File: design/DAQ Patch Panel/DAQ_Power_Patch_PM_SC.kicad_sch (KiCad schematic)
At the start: 8 parts, among them J1 Sensor 1 Terminal, J2 GND, J4 Voltage Input Terminal, J5 Sensor 1 Output, SW1 SW_SP3T, SW2 SW_SPDT_MSM

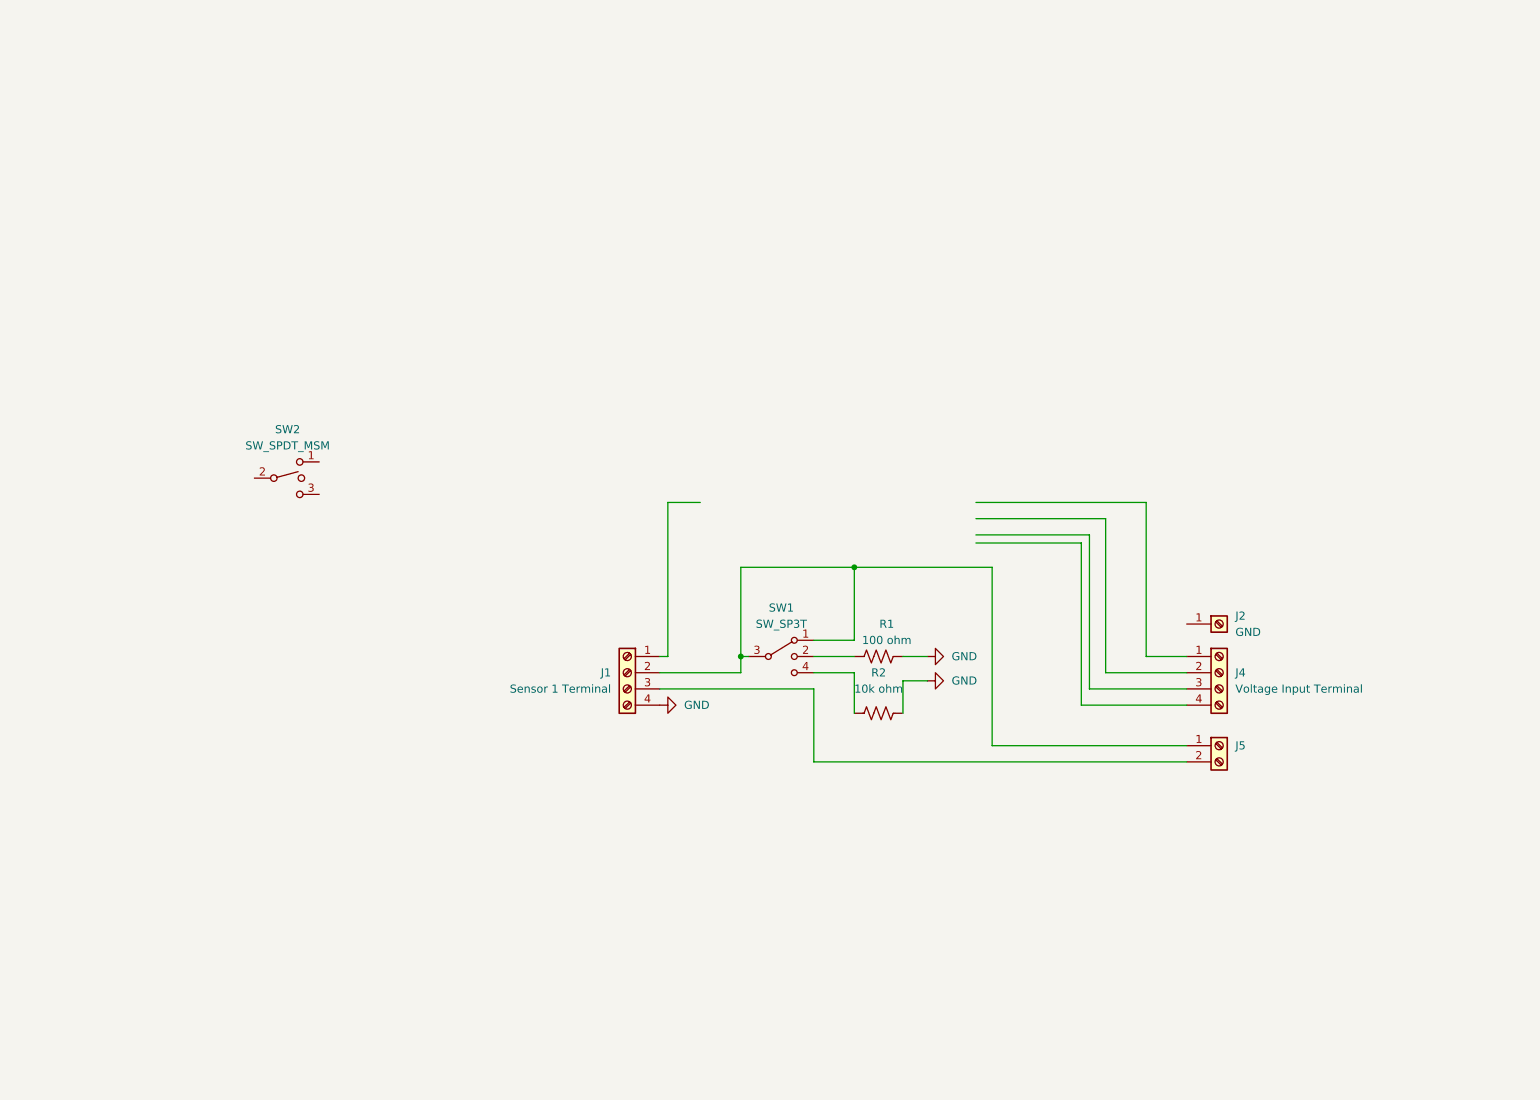
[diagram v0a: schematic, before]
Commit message: Changes to delete switches and duplicate board setup
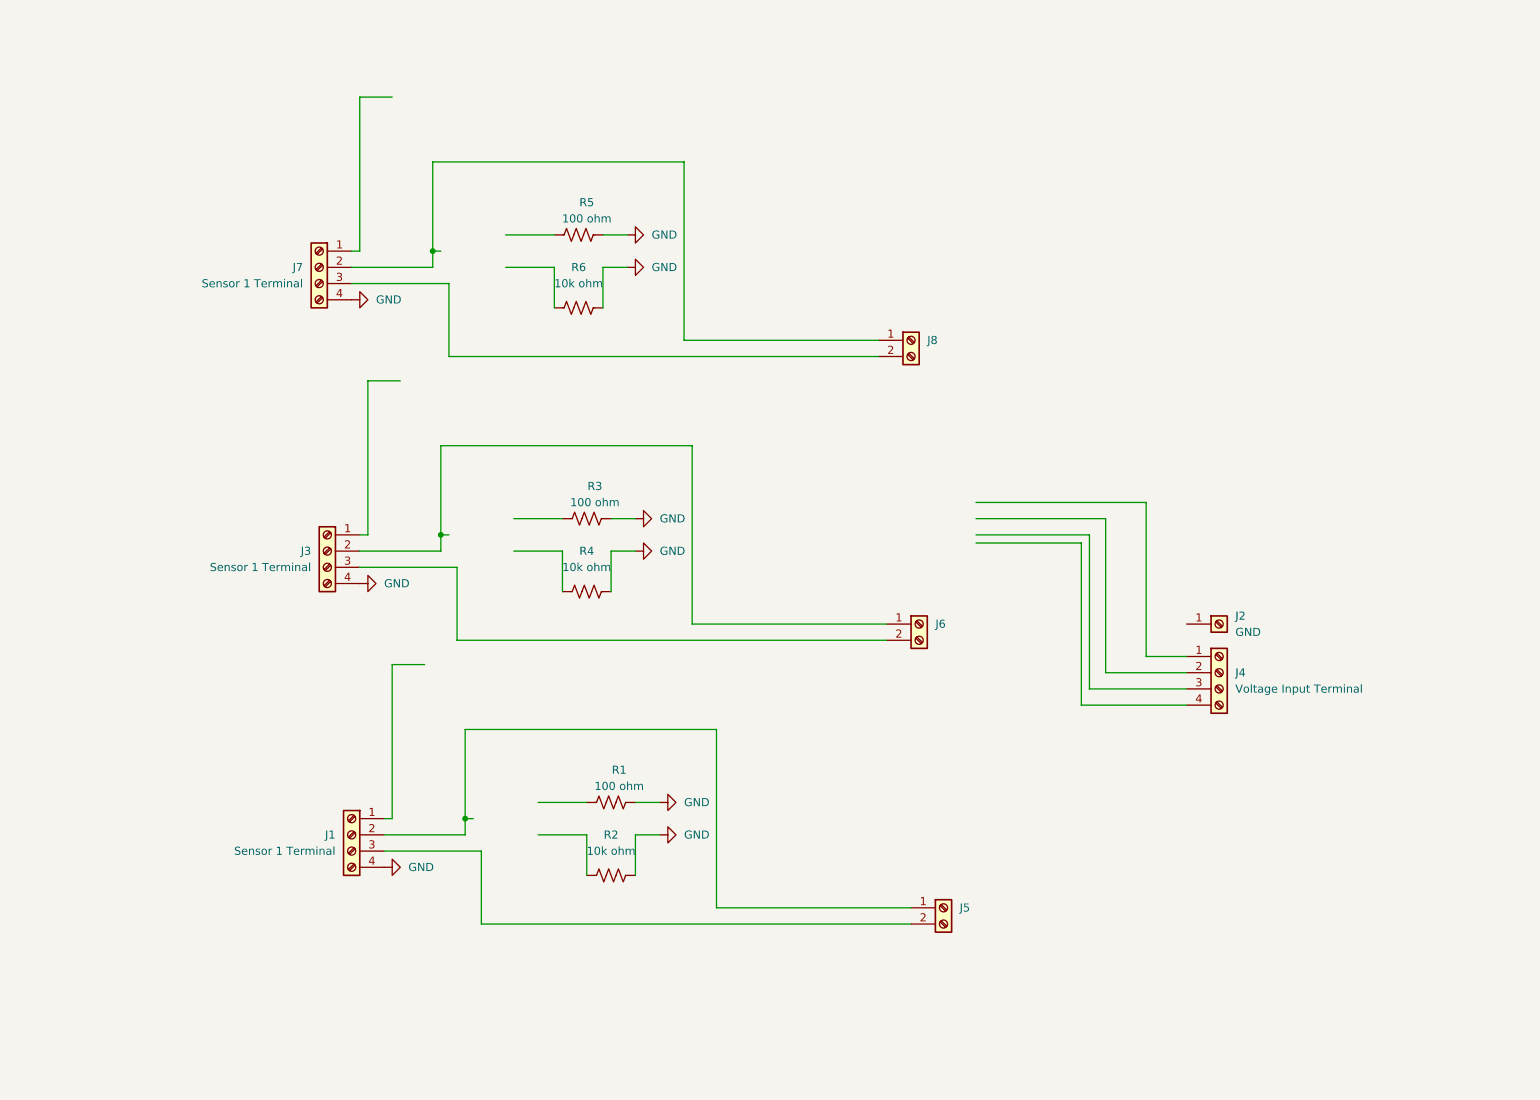
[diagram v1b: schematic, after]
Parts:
- removed SW1: SW_SP3T, symbol Switch:SW_SP3T
- removed SW2: SW_SPDT_MSM, symbol Switch:SW_SPDT_MSM
- added J3, J7: Sensor 1 Terminal, symbol Connector:Screw_Terminal_01x04
- added J6, J8: Sensor 1 Output, symbol Connector:Screw_Terminal_01x02
- added R3, R5: 100 ohm, symbol Device:R_US
- added R4, R6: 10k ohm, symbol Device:R_US
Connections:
- net GND: now also J3.4 (Pin_4), J7.4 (Pin_4), R3.2, R4.2, R5.2, R6.2
- new net: J3.2 (Pin_2), J6.1 (Pin_1)
- new net: J3.3 (Pin_3), J6.2 (Pin_2)
- new net: J7.2 (Pin_2), J8.1 (Pin_1)
- new net: J7.3 (Pin_3), J8.2 (Pin_2)
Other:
- moved on the sheet: J1, J5, R1, R2

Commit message: Added Jumpers
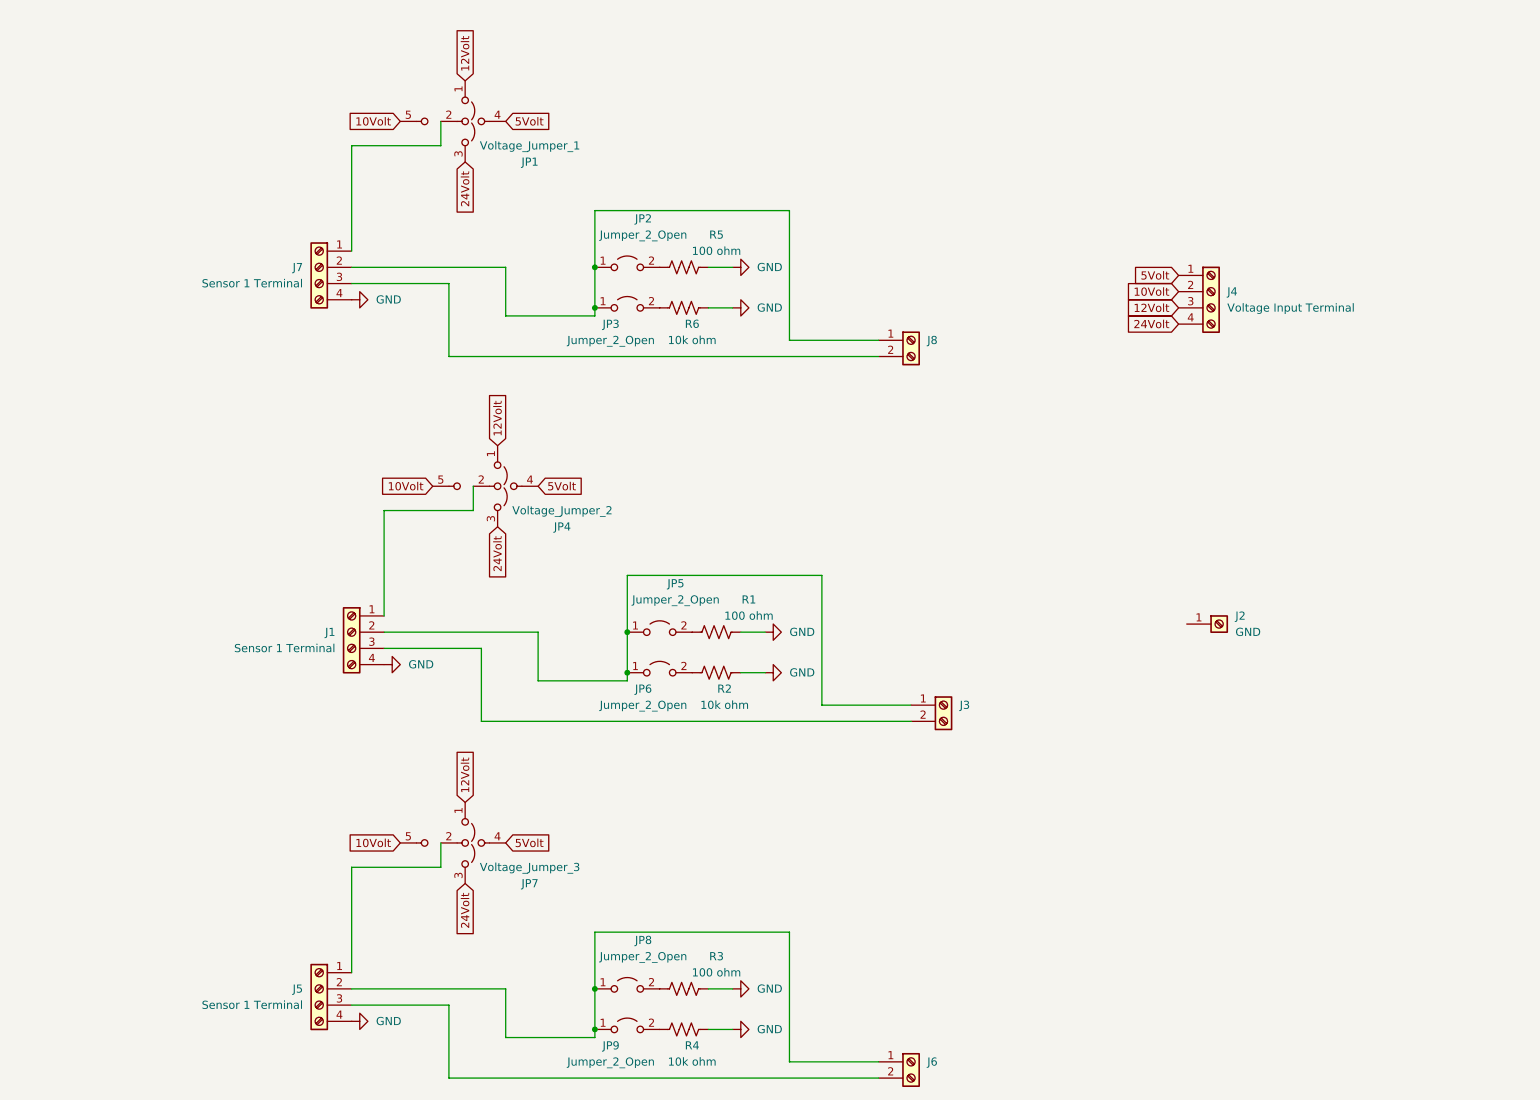
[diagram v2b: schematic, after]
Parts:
- removed J3: Sensor 1 Terminal, symbol Connector:Screw_Terminal_01x04
- removed J5: Sensor 1 Output, symbol Connector:Screw_Terminal_01x02
- added J3: Sensor 1 Output, symbol Connector:Screw_Terminal_01x02
- added J5: Sensor 1 Terminal, symbol Connector:Screw_Terminal_01x04
- added JP1: Voltage_Jumper_1, symbol Jumper:Jumper_3_Open
- added JP2, JP3, JP5, JP6, JP8, JP9: Jumper_2_Open, symbol Jumper:Jumper_2_Open
- added JP4: Voltage_Jumper_2, symbol Jumper:Jumper_3_Open
- added JP7: Voltage_Jumper_3, symbol Jumper:Jumper_3_Open
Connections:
- net GND: now also J5.4 (Pin_4)
- net 5Volt: now reaches J4.1 (Pin_1)
- net 5Volt: now also JP1.4 (C), JP4.4 (C), JP7.4 (C)
- net 10Volt: now reaches J4.2 (Pin_2)
- net 10Volt: now also JP1.5 (C), JP4.5 (C), JP7.5 (C)
- net 12Volt: now reaches J4.3 (Pin_3)
- net 12Volt: now also JP1.1 (A), JP4.1 (A), JP7.1 (A)
- net 24Volt: now reaches J4.4 (Pin_4)
- net 24Volt: now also JP1.3 (B), JP4.3 (B), JP7.3 (B)
- net at J1.2 (Pin_2): now also J3.1 (Pin_1), JP5.1 (A), JP6.1 (A)
- net at J1.3 (Pin_3): now also J3.2 (Pin_2)
- net at R2.1: now also JP6.2 (B)
- net at J6.1 (Pin_1): now also J5.2 (Pin_2), JP8.1 (A), JP9.1 (A)
- net at J6.2 (Pin_2): now also J5.3 (Pin_3)
- net at J1.1 (Pin_1): now also JP4.2 (C)
- net at J7.2 (Pin_2), J8.1 (Pin_1): now also JP2.1 (A), JP3.1 (A)
- net at R1.1: now also JP5.2 (B)
- net at R3.1: now also JP8.2 (B)
- net at R4.1: now also JP9.2 (B)
- net at R5.1: now also JP2.2 (B)
- net at R6.1: now also JP3.2 (B)
- net at J7.1 (Pin_1): now also JP1.2 (C)
- new net: J5.1 (Pin_1), JP7.2 (C)
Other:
- moved on the sheet: J4, R5, R6

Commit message: Connection for 2 thermistors or 4-20 amp sensors
Added option for 4th connector to also be power port and doubled resistors to allow for two thermistors or 4-20 amp sensors
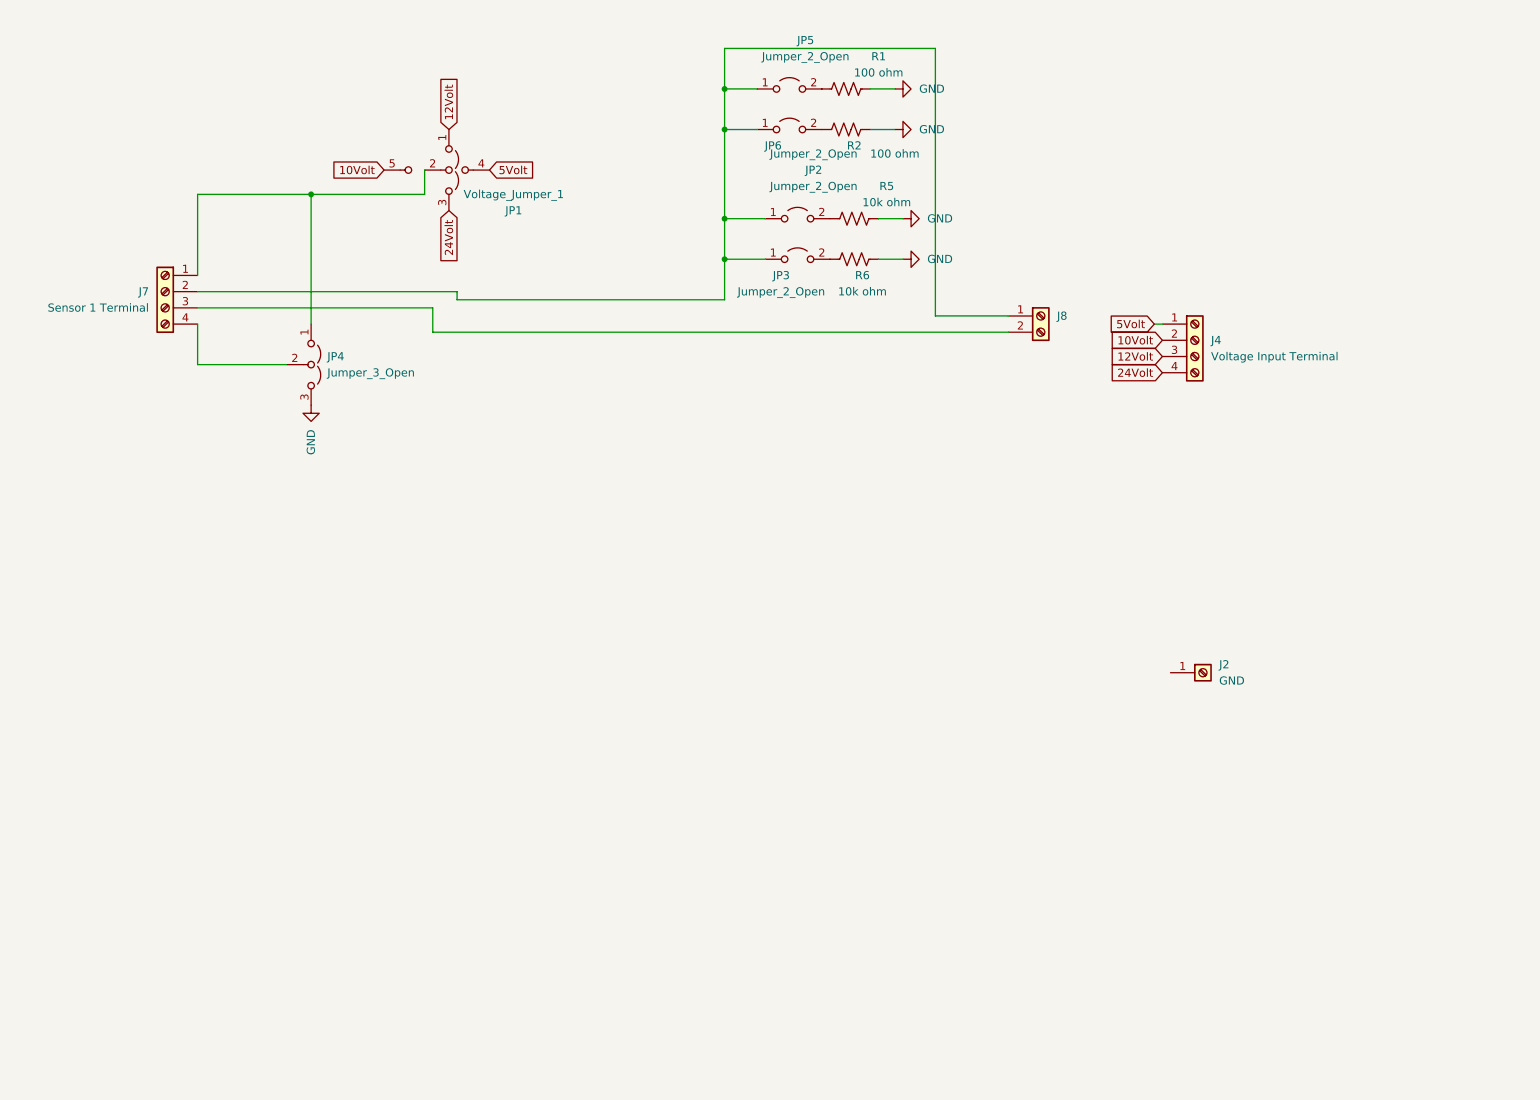
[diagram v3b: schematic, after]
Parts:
- removed J1, J5: Sensor 1 Terminal, symbol Connector:Screw_Terminal_01x04
- removed J3, J6: Sensor 1 Output, symbol Connector:Screw_Terminal_01x02
- removed JP7: Voltage_Jumper_3, symbol Jumper:Jumper_3_Open
- removed JP8, JP9: Jumper_2_Open, symbol Jumper:Jumper_2_Open
- removed R3: 100 ohm, symbol Device:R_US
- removed R4: 10k ohm, symbol Device:R_US
- JP4: value Voltage_Jumper_2 -> Jumper_3_Open
- R2: value 10k ohm -> 100 ohm
- R5: value 100 ohm -> 10k ohm
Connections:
- net 10Volt: no longer JP4.5 (C)
- net 12Volt: no longer JP4.1 (A)
- net 24Volt: no longer JP4.3 (B)
- net 5Volt: no longer JP4.4 (C)
- net GND: now also JP4.3 (B); no longer J7.4 (Pin_4)
- net at J7.2 (Pin_2), J8.1 (Pin_1), JP2.1 (A)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: now also JP5.1 (A), JP6.1 (A)
- net at JP4.2 (C): now also J7.4 (Pin_4)
- net at J7.1 (Pin_1), JP1.2 (C): now also JP4.1 (A)
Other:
- company: (none) -> Waterloo Rocketry 
- title: (none) -> DAQ_PATCH_PANEL
- moved on the sheet: J2, J4, J7, J8, JP1, JP2, JP3, R5, R6

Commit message: Added Netlabels and Fuse
Cleaned up the schematic and added a 50mA fuse to the power lines
Still need to rename jumpers and add RC low pass filter to data lines
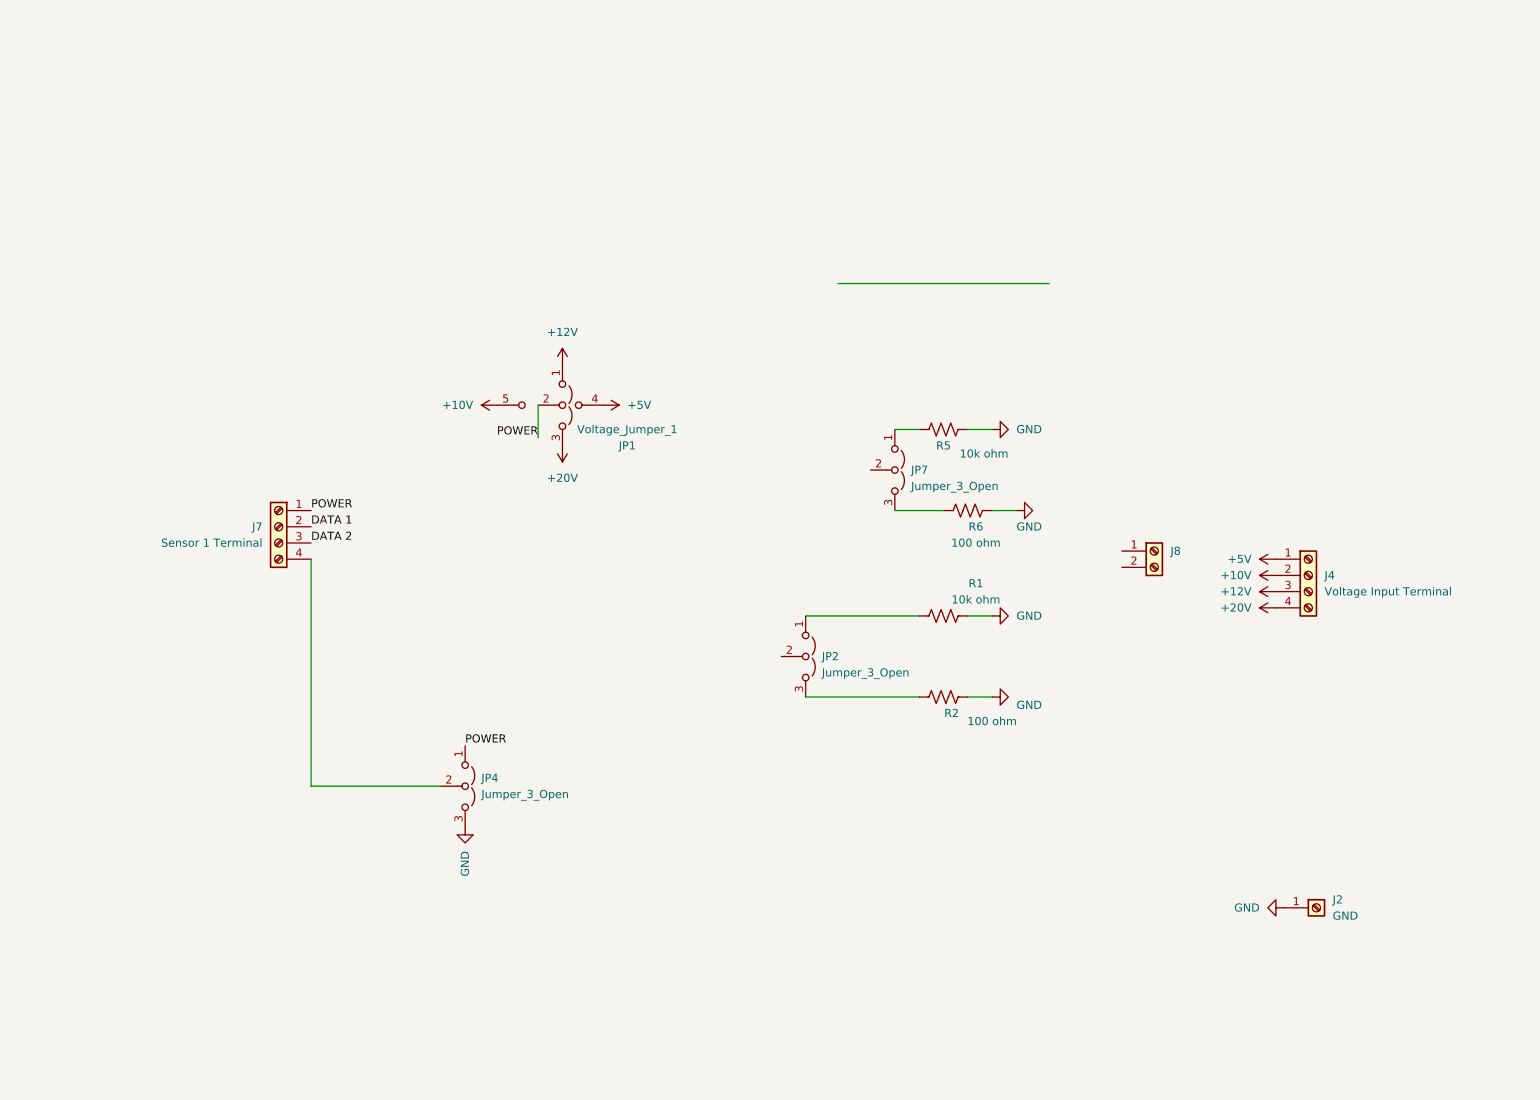
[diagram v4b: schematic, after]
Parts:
- removed JP2, JP3, JP5, JP6: Jumper_2_Open, symbol Jumper:Jumper_2_Open
- added JP2, JP7: Jumper_3_Open, symbol Jumper:Jumper_3_Open
- R1: value 100 ohm -> 10k ohm
- R6: value 10k ohm -> 100 ohm
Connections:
- net GND: now also J2.1 (Pin_1)
- net at J8.1 (Pin_1): no longer J7.2 (Pin_2)
- net at R6.1: now also JP7.3 (B)
- net at R5.1: now also JP7.1 (A)
- net at R1.1: now also JP2.1 (A)
- net POWER: now reaches J7.1 (Pin_1), JP1.2 (C), JP4.1 (A)
- net at J8.2 (Pin_2): no longer J7.3 (Pin_3)
- net at R2.1: now also JP2.3 (B)
- net 10Volt renamed +10V
- net 12Volt renamed +12V
- net 24Volt renamed +20V
- net 5Volt renamed +5V
- new net DATA 1: J7.2 (Pin_2)
- new net DATA 2: J7.3 (Pin_3)
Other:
- moved on the sheet: J2, J4, J7, J8, JP1, JP4, R1, R2, R5, R6
